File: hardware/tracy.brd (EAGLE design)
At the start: 58.5 x 38 mm, 77 parts, among them IC1 SIM900, J1 U.FL, J2 U.FL, Q4 si2305cd, T2 BC846, U1 SPX5205 3v3, U2 3339, U3 TC1014 2V8, Y1 32768Hz CFPX-217 12.5pF

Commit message: checks
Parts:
- removed R2: 2k2, rcl:R0805W
- removed R7: 470, rcl:R0805W
- removed TP1: TPTP12R, testpad:TP12R
- added R8: 330, rcl:R0805W
- added T1: BC846, transistor:SOT23
- C11: value 220nF -> 10uF
- C18: value NA 100nF -> DNP 100nF
- R21: value 100k -> 10k
- R24: value 240k -> 240K
- R4: value 240k -> 1M3
- R5: value 4k7 -> 1k
- moved R23 16.3 mm to (7.90, 28.1), flipped to the bottom, turned to 270 degrees
- moved TP5 7.57 mm to (12.6, 34.8)
- moved C11 5.00 mm to (24.7, 29.6), turned to 0 degrees
- moved R5 2.97 mm to (24.7, 25.4)
- moved TP4 2.20 mm to (52.3, 1.90)
- moved TP6 2.20 mm to (52.3, 1.90)
- moved C9 1.42 mm to (13.6, 32.2), turned to 270 degrees
- moved R35 1.22 mm to (24.7, 23.3)
- moved U$2 0.40 mm to (18.5, 33.9)
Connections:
- removed net 41: U$1.41
- removed net N$5: R2.2, U$1.34, U$2.1
- removed net VBACKUP: R1.2, U$1.35, U2.4
- new net 43: U$1.43
- new net GPS_BKP: R8.2, U$1.35
- new net N$11: C11.1, R1.2, R8.1, U2.4
- net CH: now also U$6.9; no longer R7.2
- net GND: now also T1.2, U$1.39, U$1.41; no longer R2.1
- net GPRS_EN: now also U$1.22; no longer U$1.21
- net GPRS_POW: now also U$1.21; no longer U$1.22
- net N$10: now also U$1.34, U$2.1; no longer R7.1, U$6.9
- net N$48: now also T1.3; no longer R23.2
- net N$7: now also R23.2, T1.1; no longer C11.1, U$1.43
- net VBAT: no longer TP1.TP
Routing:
- net VBACKUP: track 30.9 -> 0.00 mm
- net N$11: track 0.00 -> 22.6 mm
- net N$48: track 4.23 -> 16.6 mm, vias 0 -> 1
- net GPRS_EN: track 17.3 -> 5.74 mm, vias 1 -> 0
- net GPS_BKP: track 0.00 -> 7.98 mm
- net CH: track 17.0 -> 22.8 mm
- net N$5: track 4.94 -> 0.00 mm
- net GND: track 14.8 -> 16.7 mm, vias 64 -> 98
- net PW_EN: track 4.96 -> 6.46 mm
- net VIN: track 70.4 -> 68.9 mm
- net N$12: track 39.9 -> 38.7 mm
- net GPRS_POW: track 28.6 -> 29.8 mm
- net TEST: track 19.0 -> 20.1 mm
- net 3V3_EN: track 36.2 -> 37.3 mm
- net N$7: track 3.28 -> 2.44 mm
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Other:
- board text added: "Petre Rodan 201405 rev1"
- board text removed: "Vbat"
- board text removed: "peter 201401 rev1"

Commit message: foo
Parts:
- removed U$20: prog, Simplex-Connectors:0530470610
- added X1: MOLEX_6VERTICAL, Simplex-Connectors:0530470610
- D1: value DIODE-SCHOTTKY_ -> 15MQ040N
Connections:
- net GPRS_EN renamed GPRS_VBAT
- net GPRS_POW renamed GPRS_PWRKEY
- net 2V8: now also X1.4; no longer U$20.4
- net GND: now also X1.1; no longer U$20.1
- net P4.0: now also X1.5; no longer U$20.5
- net P4.1: now also X1.6; no longer U$20.6
- net RST: now also X1.2; no longer U$20.2
- net TEST: now also X1.3; no longer U$20.3
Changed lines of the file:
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@@
 <layer number="38" name="bTest" color="7" fill="1" visible="no" active="yes"/>
 <layer number="39" name="tKeepout" color="4" fill="11" visible="no" active="yes"/>
-<layer number="40" name="bKeepout" color="1" fill="11" visible="yes" active="yes"/>
+<layer number="40" name="bKeepout" color="1" fill="11" visible="no" active="yes"/>
 <layer number="41" name="tRestrict" color="4" fill="10" visible="no" active="yes"/>
-<layer number="42" name="bRestrict" color="1" fill="10" visible="yes" active="yes"/>
+<layer number="42" name="bRestrict" color="1" fill="10" visible="no" active="yes"/>
 <layer number="43" name="vRestrict" color="2" fill="10" visible="no" active="yes"/>
 <layer number="44" name="Drills" color="7" fill="1" visible="no" active="yes"/>
@@
 <wire x1="0" y1="38" x2="0" y2="0" width="0.4064" layer="20"/>
 <text x="30.2" y="1.7" size="1.01" layer="109" font="vector" ratio="15" rot="MR0"></text>
-<hole x="3.1" y="34.9" drill="3.5"/>
-<hole x="55.4" y="3.1" drill="3.5"/>
+<hole x="3.1" y="34.9" drill="3.2"/>
+<hole x="55.4" y="3.1" drill="3.2"/>
 <wire x1="56.4" y1="30.25" x2="55.1" y2="30.25" width="1.6764" layer="42"/>
 <rectangle x1="19.7" y1="6.5" x2="21.2" y2="8" layer="30"/>
@@
 <element name="C32" library="rcl" package="C0805" value="1uF" x="3.1" y="1.9" rot="R180"/>
 <element name="U$2" library="Simplex-rlc" package="YC164" value="470" x="18.5" y="33.9" rot="MR90"/>
-<element name="D1" library="SparkFun-DiscreteSemi" package="SMA-DIODE" value="DIODE-SCHOTTKY_" x="27.8" y="4.8" rot="MR0"/>
+<element name="D1" library="SparkFun-DiscreteSemi" package="SMA-DIODE" value="15MQ040N" x="27.8" y="4.8" rot="MR0"/>
 <element name="R3" library="rcl" package="R0805W" value="2M" x="18.9" y="10.9" rot="MR180"/>
 <element name="R4" library="rcl" package="R0805W" value="1M3" x="18.9" y="13" rot="MR0"/>
@@
 <element name="U$17" library="Simplex-Connectors" package="0530480401" value="5V" x="32.3" y="2"/>
 <element name="U$19" library="Simplex-Connectors" package="0530480401" value="LiPo" x="25.4" y="2"/>
-<element name="U$20" library="Simplex-Connectors" package="0530470610" value="prog" x="34.4" y="14" rot="MR90"/>
 <element name="R6" library="rcl" package="R0805W" value="100k" x="7.9" y="32.2" rot="MR270"/>
 <element name="LED1" library="led" package="CHIPLED_0805" value="green" x="9.6" y="32.2" rot="MR0"/>
@@
 <element name="R8" library="rcl" package="R0805W" value="330" x="24.7" y="27.5" rot="MR0"/>
 <element name="T1" library="transistor" package="SOT23" value="BC846" x="7.9" y="23.9" rot="MR180"/>
+<element name="X1" library="Simplex-Connectors" package="0530470610" value="MOLEX_6VERTICAL" x="34.3" y="14" rot="MR90"/>
 </elements>
 <signals>
@@
 <via x="0.9" y="31.7" extent="1-16" drill="0.4"/>
 <via x="1" y="19.3" extent="1-16" drill="0.4"/>
-<contactref element="U$20" pad="1"/>
 <via x="4.6" y="21.4" extent="1-16" drill="0.4"/>
 <via x="15.7" y="17.3" extent="1-16" drill="0.4"/>
+<contactref element="X1" pad="1"/>
 </signal>
 <signal name="VIN">
@@
 <wire x1="15.7" y1="26.9" x2="18.4" y2="26.9" width="0.3048" layer="16"/>
 <wire x1="18.4" y1="26.9" x2="18.5" y2="26.8" width="0.3048" layer="16"/>
-<contactref element="U$20" pad="6"/>
 <wire x1="18.5" y1="26.8" x2="19" y2="26.8" width="0.3048" layer="1"/>
 <wire x1="19" y1="26.8" x2="23.5" y2="22.3" width="0.3048" layer="1"/>
@@
 <wire x1="27" y1="22" x2="27.7" y2="22" width="0.3048" layer="16"/>
 <wire x1="27.7" y1="22" x2="29.45" y2="20.25" width="0.3048" layer="16"/>
-<wire x1="29.45" y1="20.25" x2="34.4" y2="20.25" width="0.3048" layer="16"/>
+<contactref element="X1" pad="6"/>
+<wire x1="29.45" y1="20.25" x2="34.3" y2="20.25" width="0.3048" layer="16"/>
 </signal>
 <signal name="N$6">
@@
 <wire x1="23.6475" y1="19.6" x2="23.6475" y2="19.2525" width="0.3048" layer="16"/>
 <wire x1="23.6475" y1="19.2525" x2="27.65" y2="15.25" width="0.3048" layer="16"/>
-<contactref element="U$20" pad="2"/>
-<wire x1="27.65" y1="15.25" x2="34.4" y2="15.25" width="0.3048" layer="16"/>
+<contactref element="X1" pad="2"/>
+<wire x1="27.65" y1="15.25" x2="34.3" y2="15.25" width="0.3048" layer="16"/>
 </signal>
 <signal name="TEST">
@@
 <contactref element="R35" pad="1"/>
 <wire x1="19.9" y1="21.65" x2="24.45" y2="21.65" width="0.3048" layer="16"/>
-<contactref element="U$20" pad="3"/>
 <wire x1="27.2" y1="20.7" x2="28.3" y2="19.6" width="0.3048" layer="16"/>
 <wire x1="28.3" y1="19.6" x2="28.3" y2="19.1" width="0.3048" layer="16"/>
@@
 <wire x1="32.7" y1="18.5" x2="32.7" y2="16.9" width="0.3048" layer="1"/>
 <wire x1="32.7" y1="16.9" x2="33.1" y2="16.5" width="0.3048" layer="1"/>
-<wire x1="33.1" y1="16.5" x2="34.4" y2="16.5" width="0.3048" layer="1"/>
 <wire x1="24.45" y1="21.65" x2="25.7525" y2="22.9525" width="0.3048" layer="16"/>
 <wire x1="25.7525" y1="22.9525" x2="25.7525" y2="23.3" width="0.3048" layer="16"/>
+<contactref element="X1" pad="3"/>
+<wire x1="33.1" y1="16.5" x2="34.3" y2="16.5" width="0.3048" layer="1"/>
 </signal>
 <signal name="P4.0">
@@
 <wire x1="17.5" y1="26.3" x2="17.9" y2="25.9" width="0.3048" layer="16"/>
 <wire x1="17.9" y1="25.9" x2="18.5" y2="25.9" width="0.3048" layer="16"/>
-<contactref element="U$20" pad="5"/>
 <wire x1="18.5" y1="25.9" x2="18.6" y2="25.8" width="0.254" layer="1"/>
 <wire x1="18.6" y1="25.8" x2="19" y2="25.8" width="0.3048" layer="1"/>
@@
 <wire x1="29.4" y1="19.4" x2="33.3" y2="19.4" width="0.3048" layer="16"/>
 <wire x1="33.3" y1="19.4" x2="33.7" y2="19" width="0.3048" layer="16"/>
-<wire x1="33.7" y1="19" x2="34.4" y2="19" width="0.3048" layer="16"/>
+<contactref element="X1" pad="5"/>
+<wire x1="33.7" y1="19" x2="34.3" y2="19" width="0.3048" layer="16"/>
 </signal>
 <signal name="N$31">
@@
 <wire x1="2.0475" y1="6.1" x2="2.0475" y2="4" width="0.3048" layer="1"/>
 </signal>
-<signal name="GPRS_POW">
+<signal name="GPRS_PWRKEY">
 <contactref element="R20" pad="2"/>
 <via x="4.9" y="4" extent="1-16" drill="0.4"/>
@@
 <wire x1="36.05" y1="4.25" x2="35.5" y2="4.8" width="0.8128" layer="16"/>
 </signal>
-<signal name="GPRS_EN">
+<signal name="GPRS_VBAT">
 <contactref element="R23" pad="1"/>
 <contactref element="U$1" pad="22"/>
@@
 <wire x1="17.3" y1="25.7" x2="15.3" y2="25.7" width="0.3048" layer="16"/>
 <wire x1="15.3" y1="25.7" x2="14.25" y2="26.75" width="0.3048" layer="16"/>
-<contactref element="U$20" pad="4"/>
 <wire x1="24.2" y1="19.6" x2="26.9" y2="19.6" width="0.3048" layer="1"/>
 <wire x1="26.9" y1="19.6" x2="27.2" y2="19.3" width="0.3048" layer="1"/>
@@
 <wire x1="26.9" y1="19.6" x2="27.2" y2="19.3" width="0.3048" layer="16"/>
 <wire x1="27.2" y1="19.3" x2="28.75" y2="17.75" width="0.3048" layer="16"/>
-<wire x1="28.75" y1="17.75" x2="34.4" y2="17.75" width="0.3048" layer="16"/>
 <wire x1="9.85" y1="16.5" x2="10.4" y2="16.5" width="0.3048" layer="16"/>
 <wire x1="10.4" y1="16.5" x2="12.1" y2="18.2" width="0.3048" layer="16"/>
@@
 <wire x1="14.35" y1="30.4" x2="13.6" y2="31.15" width="0.3048" layer="16"/>
 <wire x1="13.6" y1="31.15" x2="13.6" y2="31.25" width="0.3048" layer="16"/>
+<contactref element="X1" pad="4"/>
+<wire x1="28.75" y1="17.75" x2="34.3" y2="17.75" width="0.3048" layer="16"/>
 </signal>
 <signal name="N$4">
@@
 <via x="11.3" y="29" extent="1-16" drill="0.4"/>
 <via x="10" y="22.9" extent="1-16" drill="0.4"/>
-<wire x1="10" y1="22.9" x2="10.5" y2="23.9" width="0.3048" layer="1"/>
-<wire x1="10.5" y1="23.9" x2="11.3" y2="24.7" width="0.3048" layer="1"/>
 <wire x1="11.3" y1="24.7" x2="11.3" y2="29" width="0.3048" layer="1"/>
 <wire x1="9.6" y1="31.15" x2="9.6" y2="31.1" width="0.3048" layer="16"/>
 <wire x1="9.6" y1="31.1" x2="11.3" y2="29.4" width="0.3048" layer="16"/>
 <wire x1="11.3" y1="29.4" x2="11.3" y2="29" width="0.3048" layer="16"/>
+<wire x1="10" y1="22.9" x2="10" y2="24.1" width="0.3048" layer="1"/>
+<wire x1="10" y1="24.1" x2="10.6" y2="24.7" width="0.3048" layer="1"/>
+<wire x1="10.6" y1="24.7" x2="11.3" y2="24.7" width="0.3048" layer="1"/>
 </signal>
 <signal name="N$8">
@@
 <contactref element="U$1" pad="15"/>
 <via x="9.9" y="22" extent="1-16" drill="0.4"/>
-<wire x1="9.9" y1="22" x2="10.1" y2="21.9" width="0.3048" layer="1"/>
-<wire x1="10.1" y1="21.9" x2="10.9" y2="21.1" width="0.3048" layer="1"/>
-<wire x1="10.9" y1="21.1" x2="10.9" y2="13.7" width="0.3048" layer="1"/>
+<wire x1="10.9" y1="20.1" x2="10.9" y2="13.7" width="0.3048" layer="1"/>
 <wire x1="11.3" y1="22.15" x2="10.05" y2="22.15" width="0.3048" layer="16"/>
 <wire x1="10.05" y1="22.15" x2="9.9" y2="22" width="0.3048" layer="16"/>
@@
 <wire x1="17.8" y1="8.9" x2="16.1" y2="8.9" width="0.3048" layer="1"/>
 <wire x1="16.1" y1="8.9" x2="15.9" y2="8.7" width="0.3048" layer="1"/>
+<wire x1="9.9" y1="22" x2="9.9" y2="21.1" width="0.3048" layer="1"/>
+<wire x1="9.9" y1="21.1" x2="10.9" y2="20.1" width="0.3048" layer="1"/>
 </signal>
 <signal name="43">

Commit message: keepout under fuse
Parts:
- C18: value DNP 100nF -> 47nF
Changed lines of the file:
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@@
 <layer number="40" name="bKeepout" color="1" fill="11" visible="no" active="yes"/>
 <layer number="41" name="tRestrict" color="4" fill="10" visible="no" active="yes"/>
-<layer number="42" name="bRestrict" color="1" fill="10" visible="no" active="yes"/>
+<layer number="42" name="bRestrict" color="1" fill="10" visible="yes" active="yes"/>
 <layer number="43" name="vRestrict" color="2" fill="10" visible="no" active="yes"/>
 <layer number="44" name="Drills" color="7" fill="1" visible="no" active="yes"/>
@@
 <wire x1="3.7" y1="23" x2="6.5" y2="23" width="1.6764" layer="41"/>
 <rectangle x1="18" y1="5.1" x2="21.8" y2="9.4" layer="30"/>
+<wire x1="34" y1="5.5" x2="34" y2="4" width="1.4224" layer="42"/>
 </plain>
 <attributes>
@@
 <element name="C8" library="rcl" package="C0805" value="100nF" x="9.8" y="17.4" rot="MR270"/>
 <element name="C9" library="rcl" package="C0805" value="100nF" x="13.6" y="32.2" rot="MR270"/>
-<element name="C18" library="rcl" package="C0805" value="DNP 100nF" x="23" y="15.1" rot="MR180"/>
+<element name="C18" library="rcl" package="C0805" value="47nF" x="23" y="15.1" rot="MR180"/>
 <element name="R1" library="rcl" package="R0805W" value="4k7" x="38.2" y="19.8" rot="MR90"/>
 <element name="U$5" library="Simplex-rlc" package="L0805W" value="bead" x="52" y="11.1" rot="MR90"/>

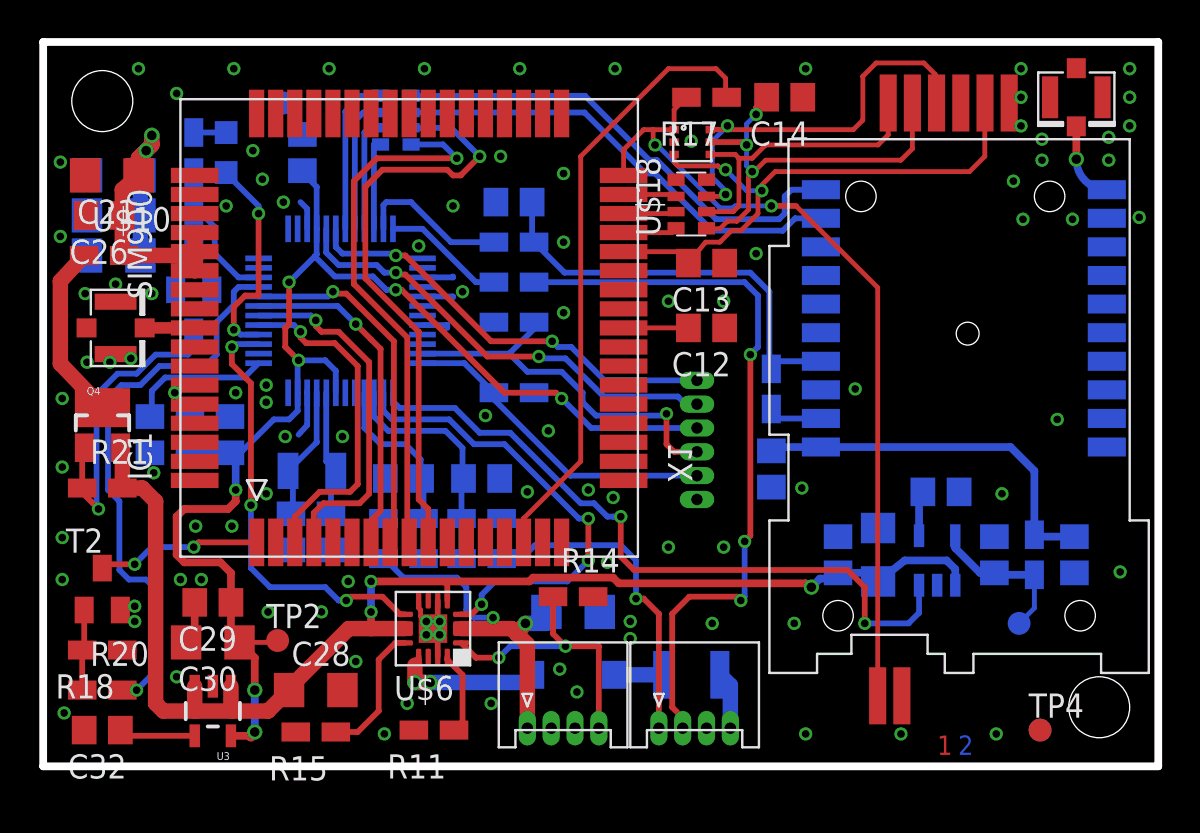
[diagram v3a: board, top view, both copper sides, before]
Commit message: add fram buffer
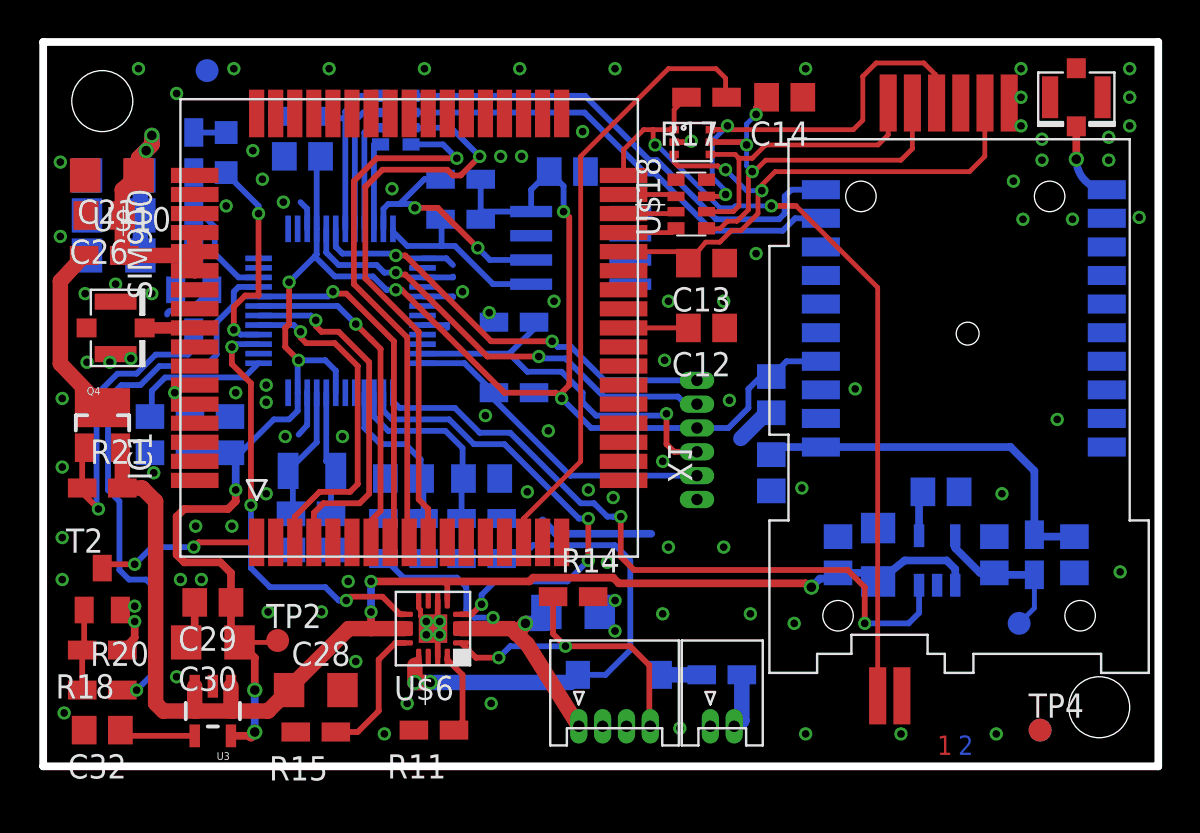
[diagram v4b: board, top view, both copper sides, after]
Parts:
- removed R8: 330, rcl:R0805W
- added C19: 100nF, rcl:C0805
- added R2: 6K2, rcl:R0805W
- added X2: MOLEX_2HORIZONTAL, Simplex-Connectors:0530480210
- R5: value 1k -> 4k7
- U$17: value 5V -> FM24V; device Simplex-Connectors:0530480401 -> Simplex-ICs:SO-08
- U$9: value RESETTABLE -> RESETTABLE_0805; device Simplex-Fuses:1210 -> Simplex-Fuses:0805W
- moved U$17 25.5 mm to (28.2, 27.2), flipped to the bottom, turned to 270 degrees
- moved R1 19.7 mm to (21.9, 30.8), turned to 180 degrees
- moved C11 16.9 mm to (38.2, 19.5), turned to 270 degrees
- moved TP5 4.35 mm to (8.60, 36.5)
- moved R5 4.33 mm to (21.9, 28.7), turned to 180 degrees
- moved U$19 2.70 mm to (28.1, 2.10)
- moved D1 2.40 mm to (30.2, 4.80)
- moved U$9 1.60 mm to (35.6, 4.80)
- moved C9 0.20 mm to (13.6, 32.0), turned to 180 degrees
- moved C7 0.20 mm to (38.2, 15.4)
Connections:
- net PW_RAW_DIV renamed 5V_DIV
- removed net GPS_BKP: R8.2, U$1.35
- removed net N$11: C11.1, R1.2, R8.1, U2.4
- removed net N$12: R5.1, U$17.2
- removed net N$31: R1.1, U2.2
- removed net PW_EN: R5.2, U$1.36
- removed net PW_RAW: R22.1, U$17.1
- new net SCL_FM: R1.1, U$1.35, U$17.6
- new net SDA_FM: R5.1, U$1.36, U$17.5
- net 2V8: now also C11.1, C19.1, R1.2, R5.2, U$17.8, U2.4
- net 5V: now also U$9.1, X2.2; no longer U$17.4, U$9.P$1
- net 5V_IN: now also R22.1
- net GND: now also C19.2, R2.1, U$17.2, U$17.4, X2.1
- net N$20: now also U$9.2; no longer U$9.P$2
- net N$3: now also R2.2
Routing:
- net N$12: track 38.7 -> 0.00 mm, vias 3 -> 0
- net 2V8: track 72.8 -> 102.6 mm, vias 7 -> 8
- net N$11: track 22.6 -> 0.00 mm
- net 5V_IN: track 8.37 -> 26.1 mm
- net PW_RAW: track 17.2 -> 0.00 mm, vias 1 -> 0
- net GND: track 16.7 -> 33.0 mm, vias 98 -> 101
- net SCL_FM: track 0.00 -> 12.8 mm, vias 0 -> 2
- net SDA_FM: track 0.00 -> 9.96 mm
- net GPS_BKP: track 7.98 -> 0.00 mm
- net PW_EN: track 6.46 -> 0.00 mm
- net N$31: track 3.10 -> 0.00 mm
- net TS: track 15.0 -> 17.0 mm
- net N$3: track 8.34 -> 9.64 mm
- net BAT: track 20.6 -> 21.3 mm
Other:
- board text added: "Petre Rodan 201408 rev2"
- board text removed: "Petre Rodan 201405 rev1"

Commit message: rev 2
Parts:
- removed R17: 10k, rcl:R0805W
- removed U$19: LiPo, Simplex-Connectors:0530480401
- added R7, R8: 4k7, rcl:R0805W
- added X3: MOLEX_6HORIZONTAL, Simplex-Connectors:0530480610
- added X4: MOLEX_2HORIZONTAL, Simplex-Connectors:0530480210
- C11: value 10uF -> 1uF
- C3: device rcl:C1206 -> rcl:C0805
- U$3: value SIMLOCKC707_10M006_000_2 -> SIM_MOLEX_7880-0001; device Simplex-Connectors:SIMLOCK_C707_10M006 -> Simplex-Connectors:MOLEX_7880-0001
- X1: value MOLEX_6VERTICAL -> MOLEX_2HORIZONTAL; device Simplex-Connectors:0530470610 -> Simplex-Connectors:0530480210
- moved TP4 37.9 mm to (33.2, 34.7)
- moved TP6 37.9 mm to (33.2, 34.7)
- moved U$3 28.0 mm to (35.5, 28.5), turned to 270 degrees
- moved U$7 26.3 mm to (40.9, 34.5)
- moved C14 25.7 mm to (42.7, 9.65), turned to 0 degrees
- moved X1 12.6 mm to (38.5, 2.10), flipped to the top, turned to 180 degrees
- moved C5 9.27 mm to (45.4, 14.3), turned to 0 degrees
- moved J1 8.40 mm to (45.8, 35.3)
- moved C3 7.70 mm to (36.1, 11.1)
- moved C11 7.49 mm to (31.1, 21.9)
- moved U2 7.34 mm to (33.0, 32.2)
- moved R14 6.86 mm to (28.9, 2.14), flipped to the bottom, turned to 180 degrees
- moved U$8 6.10 mm to (39.0, 30.6)
- moved C4 5.80 mm to (41.3, 14.3)
- moved C1 5.60 mm to (44.3, 11.1)
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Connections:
- removed net N$42: IC1.34, R17.2, U$3.LOCK_1, U$8.1
- removed net N$43: IC1.15, R17.1
- net 2V8: now also R7.1, R8.1, X3.3; no longer X1.4
- net 5V: now also X1.2; no longer X2.2
- net BAT: now also X2.2; no longer U$19.1
- net GND: now also U$3.SH@1, U$3.SH@2, U$3.SH@3, U$3.SH@4, X3.6, X4.2; no longer U$19.2, U$19.3, U$3.LOCK_2
- net P4.0: now also R8.2, X3.2; no longer X1.5
- net P4.1: now also R7.2, X3.1; no longer X1.6
- net RST: now also X3.5; no longer X1.2
- net TEST: now also X3.4; no longer X1.3
- net TS: now also X4.1; no longer U$19.4
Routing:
- net N$42: track 43.5 -> 0.00 mm, vias 2 -> 0
- net P4.0: track 24.0 -> 59.7 mm, vias 2 -> 5
- net P4.1: track 22.8 -> 55.9 mm, vias 2 -> 5
- net N$43: track 32.2 -> 0.00 mm
- net 2V8: track 102.6 -> 123.0 mm, vias 8 -> 12
- net SIM_VCC: track 31.3 -> 13.8 mm, vias 2 -> 0
- net TEST: track 20.0 -> 37.5 mm
- net RST: track 17.0 -> 32.7 mm, vias 0 -> 1
- net SIMLOCK_IO: track 22.7 -> 32.7 mm, vias 3 -> 2
- net GPS_RX: track 25.4 -> 15.9 mm
- net TS: track 17.0 -> 8.43 mm, vias 2 -> 0
- net GPS_TX: track 24.3 -> 16.6 mm
- net SIMLOCK_RST: track 22.6 -> 15.4 mm
- net GND: track 33.0 -> 39.4 mm, vias 101 -> 107
- net VIN: track 68.9 -> 63.0 mm
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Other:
- board size 58.5 x 38 mm -> 50 x 38 mm
- board text added: "10KOhm ts"
- board text added: "3.7V bat"
- board text removed: "bat"
